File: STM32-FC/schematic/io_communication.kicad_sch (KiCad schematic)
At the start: 21 parts, among them J10 GH 1.25mm 6P, J11 GH 1.25mm 6P, J12 GH 1.25mm 4P, J13 GH 1.25mm 4P, J14 GH 1.25mm 4P, J15 GH 1.25mm 6P, U10 ATA6561-GBQW, U11 ATA6561-GBQW

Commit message: update : AHRS PCB layout & routing done
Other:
- note added: "* Secondary GPS only GH 1.25mm 6P GPS1_TX : PC6 : UART6_TX GPS1_RX : PC7 : UART6_RX GPS1_SCL : PB10 : I2C2_SCL GPS1_SDA : PB11 : I2C2_SDA"
- note added: "* Without hardware flow control GH 1.25mm 6P PD8 : UART3_TX PD9 : UART3_RX"
- note added: "GPS"
- note added: "TELE2"
- note removed: "GH 1.25mm 6P GPS1_TX : PC6 : UART6_TX GPS1_RX : PC7 : UART6_RX GPS1_SCL : PB10 : I2C2_SCL GPS1_SDA : PB11 : I2C2_SDA"
- note removed: "GH 1.25mm 6P PD8 : UART3_TX PD9 : UART3_RX"
- note removed: "GPS1"
- note removed: "TELE2 (No hardware flow control)"
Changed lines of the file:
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@@
 		(company "NARAE")
 		(comment 1 "INHA Univ. Areo-modelling Club")
-		(comment 2 "2024 Winter UAV Project ")
+		(comment 2 "* Work in progress")
 	)
 	(rectangle
@@
 		)
 	)
-	(text "GH 1.25mm 6P\n\nPD8 : UART3_TX\nPD9 : UART3_RX"
+	(text "* Without hardware flow control\n\nGH 1.25mm 6P\n\nPD8 : UART3_TX\nPD9 : UART3_RX"
 		(exclude_from_sim no)
 		(at 23.876 58.674 0)
@@
 		)
 	)
-	(text "GPS1"
+	(text "GPS"
 		(exclude_from_sim no)
 		(at 194.056 15.494 0)
@@
 		)
 	)
-	(text "TELE2 (No hardware flow control)"
+	(text "TELE2"
 		(exclude_from_sim no)
 		(at 23.876 56.134 0)
@@
 		)
 	)
-	(text "GH 1.25mm 6P\n\nGPS1_TX  : PC6 : UART6_TX\nGPS1_RX  : PC7 : UART6_RX\nGPS1_SCL : PB10 : I2C2_SCL\nGPS1_SDA : PB11 : I2C2_SDA"
+	(text "* Secondary GPS only\n\nGH 1.25mm 6P\n\nGPS1_TX  : PC6 : UART6_TX\nGPS1_RX  : PC7 : UART6_RX\nGPS1_SCL : PB10 : I2C2_SCL\nGPS1_SDA : PB11 : I2C2_SDA"
 		(exclude_from_sim no)
 		(at 194.056 18.034 0)

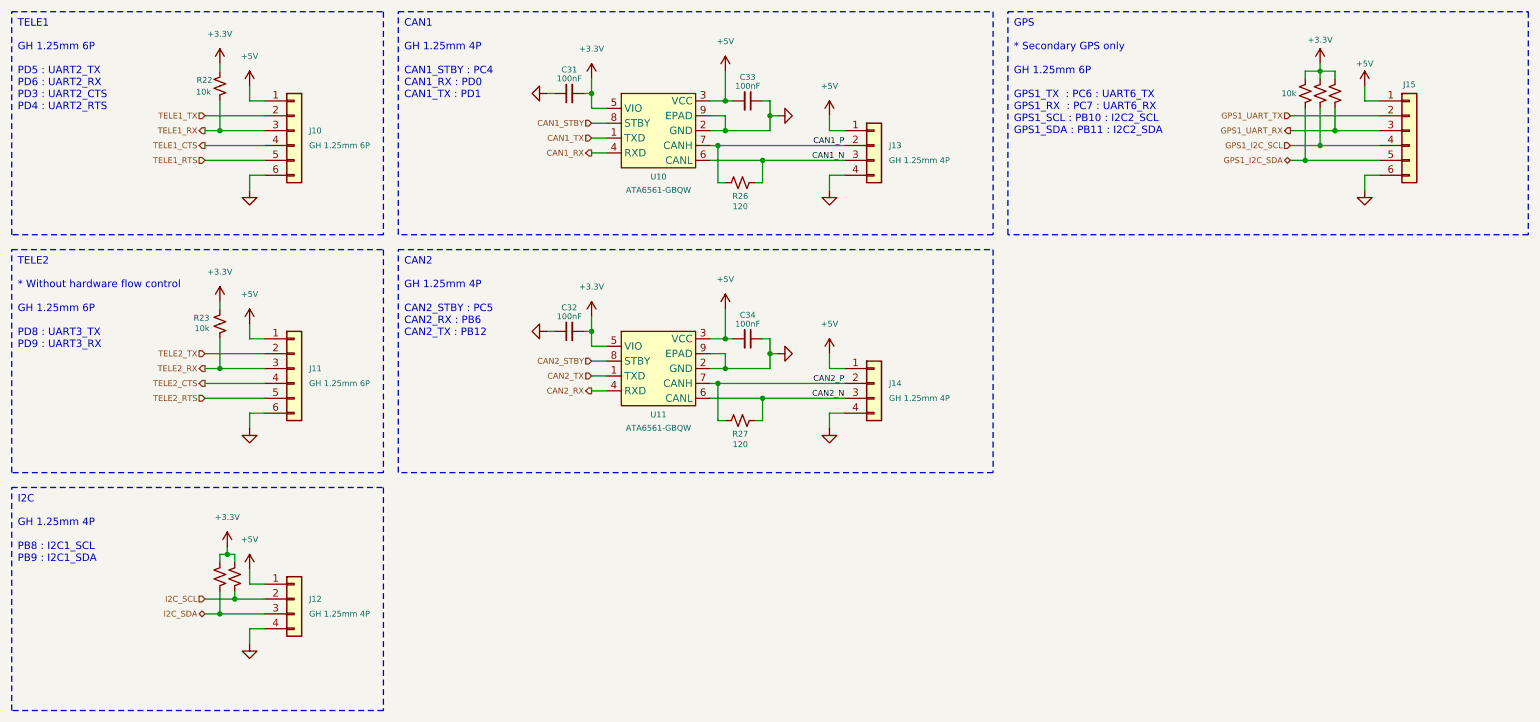
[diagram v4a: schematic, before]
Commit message: fix : readme & schematic minor fix
- schematic comment fix
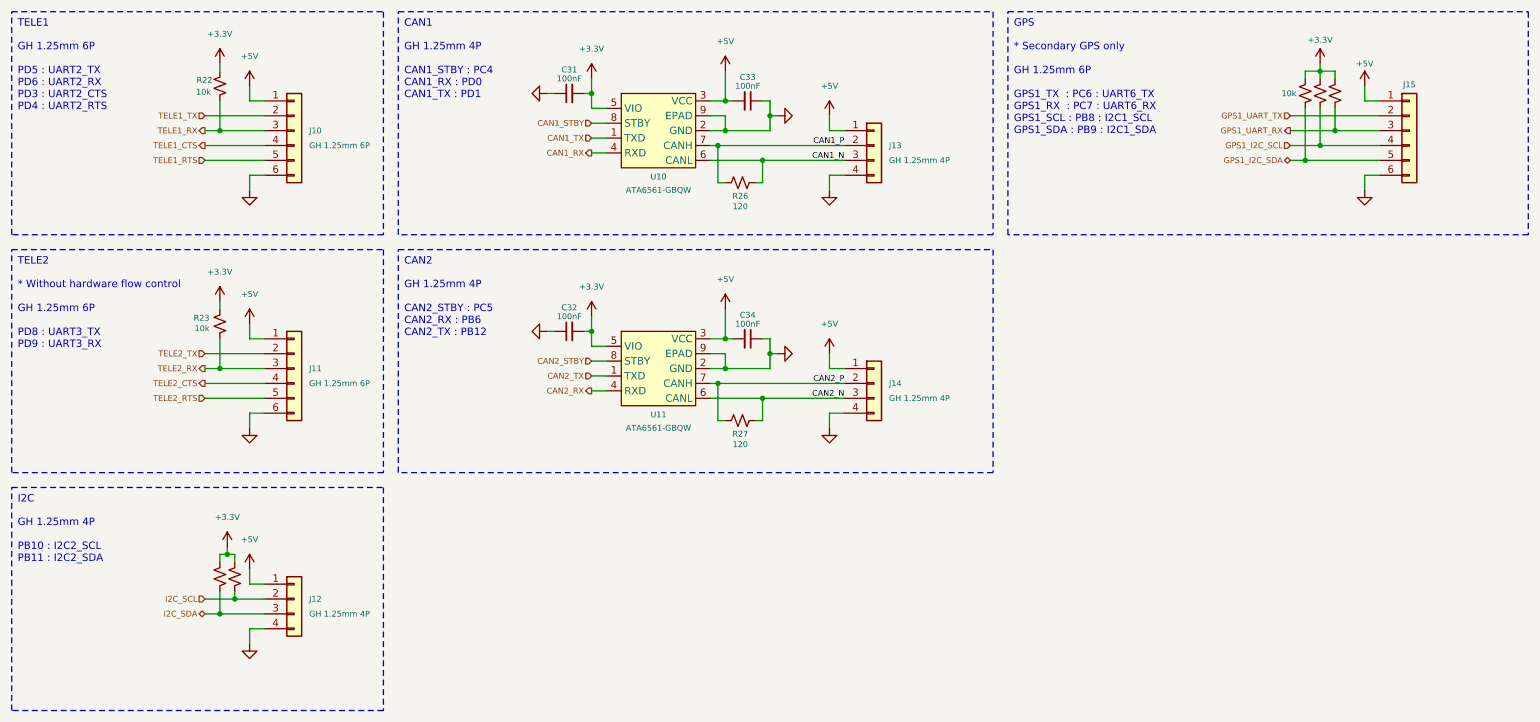
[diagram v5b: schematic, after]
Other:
- note added: "* Secondary GPS only GH 1.25mm 6P GPS1_TX : PC6 : UART6_TX GPS1_RX : PC7 : UART6_RX GPS1_SCL : PB8 : I2C1_SCL GPS1_SDA : PB9 : I2C1_SDA"
- note added: "GH 1.25mm 4P PB10 : I2C2_SCL PB11 : I2C2_SDA"
- note removed: "* Secondary GPS only GH 1.25mm 6P GPS1_TX : PC6 : UART6_TX GPS1_RX : PC7 : UART6_RX GPS1_SCL : PB10 : I2C2_SCL GPS1_SDA : PB11 : I2C2_SDA"
- note removed: "GH 1.25mm 4P PB8 : I2C1_SCL PB9 : I2C1_SDA"
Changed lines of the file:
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@@
 	(title_block
 		(title "NARAEON - Flight Controller")
-		(date "2025-10-10")
+		(date "2025-10-11")
 		(rev "v1.1.0")
 		(company "NARAE")
 		(comment 1 "INHA Univ. Areo-modelling Club")
-		(comment 2 "* Work in progress")
+		(comment 2 "github.com/NARAE-INHA-UNIV")
 	)
 	(rectangle
@@
 		)
 	)
-	(text "GH 1.25mm 4P\n\nPB8 : I2C1_SCL\nPB9 : I2C1_SDA"
+	(text "GH 1.25mm 4P\n\nPB10 : I2C2_SCL\nPB11 : I2C2_SDA"
 		(exclude_from_sim no)
 		(at 23.876 99.314 0)
@@
 		)
 	)
-	(text "* Secondary GPS only\n\nGH 1.25mm 6P\n\nGPS1_TX  : PC6 : UART6_TX\nGPS1_RX  : PC7 : UART6_RX\nGPS1_SCL : PB10 : I2C2_SCL\nGPS1_SDA : PB11 : I2C2_SDA"
+	(text "* Secondary GPS only\n\nGH 1.25mm 6P\n\nGPS1_TX  : PC6 : UART6_TX\nGPS1_RX  : PC7 : UART6_RX\nGPS1_SCL : PB8 : I2C1_SCL\nGPS1_SDA : PB9 : I2C1_SDA\n"
 		(exclude_from_sim no)
 		(at 194.056 18.034 0)
